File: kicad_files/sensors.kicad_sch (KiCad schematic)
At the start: 41 parts, among them J1 Conn_01x01_Socket, J2 U.FL, U2 MS5611-01BA, U3 BMI088, U4 MMC5983MA, U5 MAX-M10S, U6 BMP388, U7 LSM6DSM

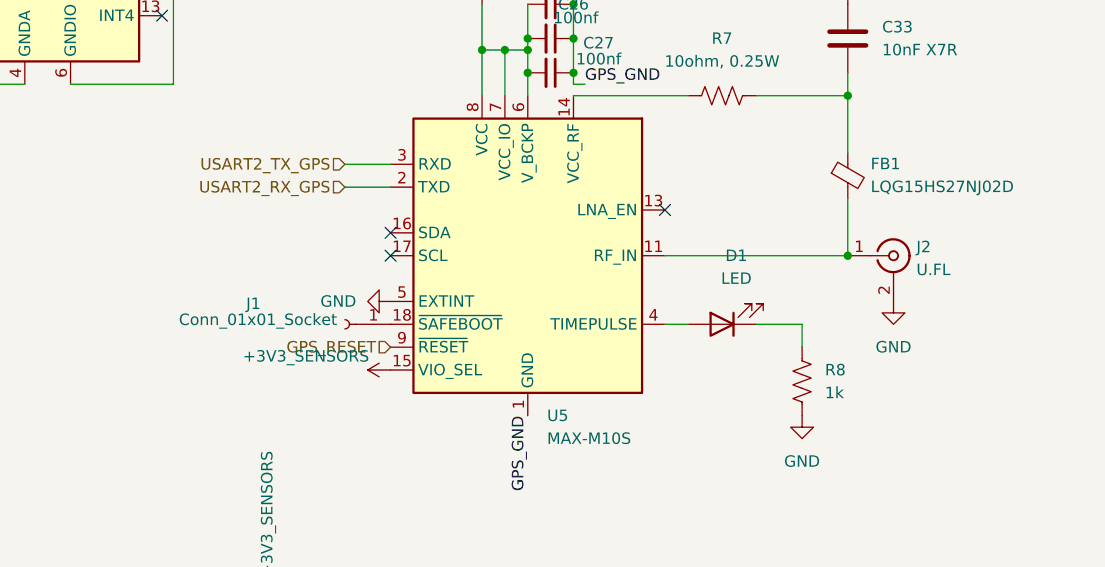
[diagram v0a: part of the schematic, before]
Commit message: size polyfuse, final drc stuff
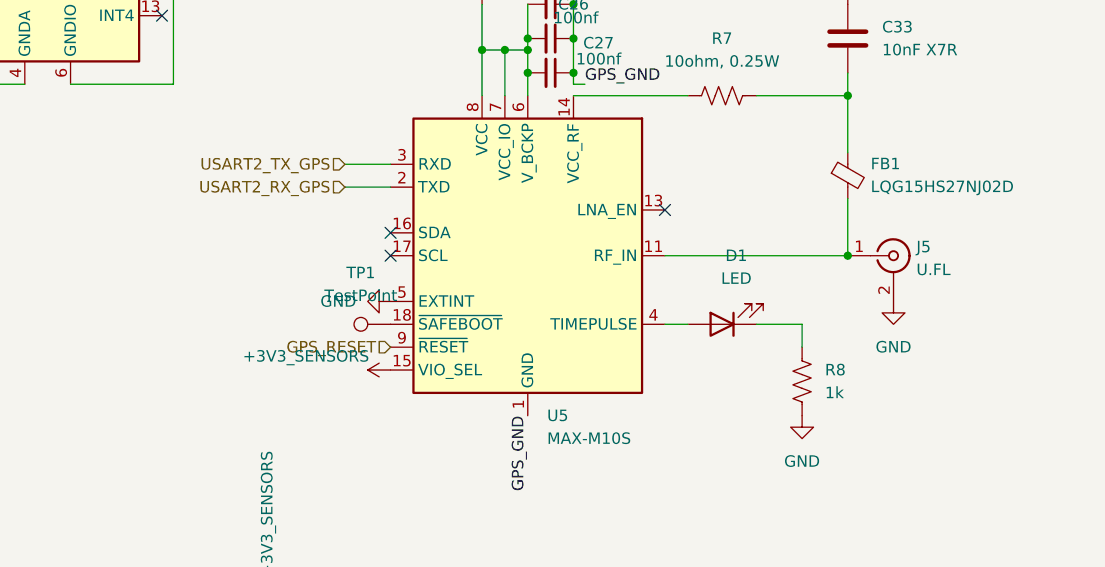
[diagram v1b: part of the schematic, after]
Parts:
- removed J1: Conn_01x01_Socket, TestPoint:TestPoint_Pad_D1.0mm, symbol Connector:Conn_01x01_Socket
- added TP1: TestPoint, TestPoint:TestPoint_Pad_D1.0mm, symbol Connector:TestPoint
- FB2: footprint Resistor_SMD:R_0603_1608Metric -> Inductor_SMD:L_0603_1608Metric
- renumbered J2 to J5
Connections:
- net at U5.18 (~{SAFEBOOT}): now also TP1.1
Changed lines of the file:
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@@
 		(dnp no)
 		(fields_autoplaced yes)
-		(property "Reference" "J2"
+		(property "Reference" "J5"
 			(at 182.88 108.2431 0)
 			(show_name no)
@@
 			(project "versorlite"
 				(path "/1a230af0-0a74-48f7-8607-b087121dda49/11200af7-3897-4179-b08c-df8c2996a93a"
-					(reference "J2")
+					(reference "J5")
 					(unit 1)
 				)
@@
 	)
 	(symbol
+		(lib_id "Connector:TestPoint")
+		(at 124.46 116.84 90)
+		(unit 1)
+		(body_style 1)
+		(exclude_from_sim no)
+		(in_bom yes)
+		(on_board yes)
+		(in_pos_files yes)
+		(dnp no)
+		(fields_autoplaced yes)
+		(property "Reference" "TP1"
+			(at 121.158 111.125 90)
+			(show_name no)
+			(do_not_autoplace no)
+			(effects
+				(font
+					(size 1.27 1.27)
+				)
+			)
+		)
+		(property "Value" "TestPoint"
+			(at 121.158 113.665 90)
+			(show_name no)
+			(do_not_autoplace no)
+			(effects
+				(font
+					(size 1.27 1.27)
+				)
+			)
+		)
+		(property "Footprint" "TestPoint:TestPoint_Pad_D1.0mm"
+			(at 124.46 111.76 0)
+			(hide yes)
+			(show_name no)
+			(do_not_autoplace no)
+			(effects
+				(font
+					(size 1.27 1.27)
+				)
+			)
+		)
+		(property "Datasheet" ""
+			(at 124.46 111.76 0)
+			(hide yes)
+			(show_name no)
+			(do_not_autoplace no)
+			(effects
+				(font
+					(size 1.27 1.27)
+				)
+			)
+		)
+		(property "Description" "test point"
+			(at 124.46 116.84 0)
+			(hide yes)
+			(show_name no)
+			(do_not_autoplace no)
+			(effects
+				(font
+					(size 1.27 1.27)
+				)
+			)
+		)
+		(pin "1"
+		)
+		(instances
+			(project "versorlite"
+				(path "/1a230af0-0a74-48f7-8607-b087121dda49/11200af7-3897-4179-b08c-df8c2996a93a"
+					(reference "TP1")
+					(unit 1)
+				)
+			)
+		)
+	)
+	(symbol
 		(lib_id "Sensor_Motion:BMI088")
 		(at 86.36 74.93 0)
@@
 			)
 		)
-		(property "Footprint" "Resistor_SMD:R_0603_1608Metric"
+		(property "Footprint" "Inductor_SMD:L_0603_1608Metric"
 			(at 229.87 135.382 90)
 			(hide yes)
@@
 					(unit 1)
 				)
-			)
-		)
-	)
-	(symbol
-		(lib_id "Connector:Conn_01x01_Socket")
-		(at 119.38 116.84 180)
-		(unit 1)
-		(body_style 1)
-		(exclude_from_sim no)
-		(in_bom yes)
-		(on_board yes)
-		(in_pos_files yes)
-		(dnp no)
-		(property "Reference" "J1"
-			(at 109.22 114.554 0)
-			(show_name no)
-			(do_not_autoplace no)
-			(effects
-				(font
-					(size 1.27 1.27)
-				)
-			)
-		)
-		(property "Value" "Conn_01x01_Socket"
-			(at 109.728 116.332 0)
-			(show_name no)
-			(do_not_autoplace no)
-			(effects
-				(font
-					(size 1.27 1.27)
-				)
-			)
-		)
-		(property "Footprint" "TestPoint:TestPoint_Pad_D1.0mm"
-			(at 119.38 116.84 0)
-			(hide yes)
-			(show_name no)
-			(do_not_autoplace no)
-			(effects
-				(font
-					(size 1.27 1.27)
-				)
-			)
-		)
-		(property "Datasheet" ""
-			(at 119.38 116.84 0)
-			(hide yes)
-			(show_name no)
-			(do_not_autoplace no)
-			(effects
-				(font
-					(size 1.27 1.27)
-				)
-			)
-		)
-		(property "Description" "Generic connector, single row, 01x01, script generated"
-			(at 119.38 116.84 0)
-			(hide yes)
-			(show_name no)
-			(do_not_autoplace no)
-			(effects
-				(font
-					(size 1.27 1.27)
-				)
-			)
-		)
-		(pin "1"
-		)
-		(instances
-			(project "versorlite"
-				(path "/1a230af0-0a74-48f7-8607-b087121dda49/11200af7-3897-4179-b08c-df8c2996a93a"
-					(reference "J1")
-					(unit 1)
-				)

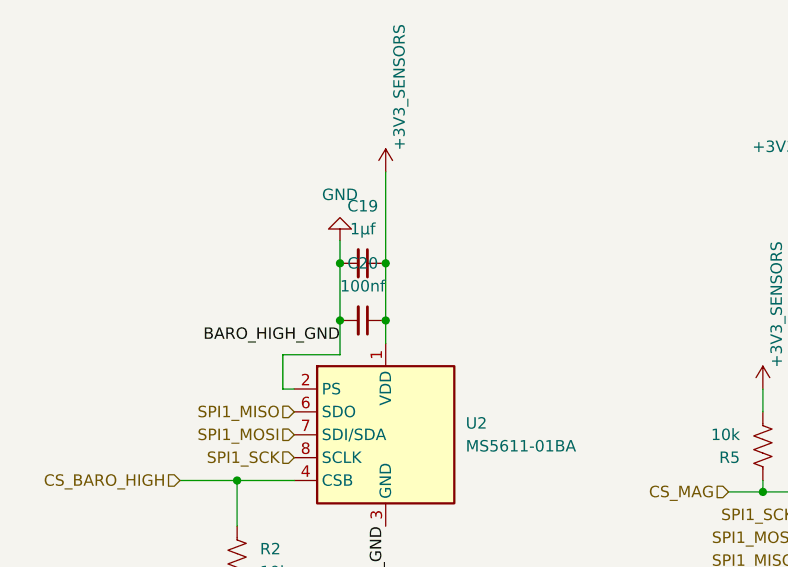
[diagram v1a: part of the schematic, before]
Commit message: better schematic labeling so that mr. dzula isn't confused
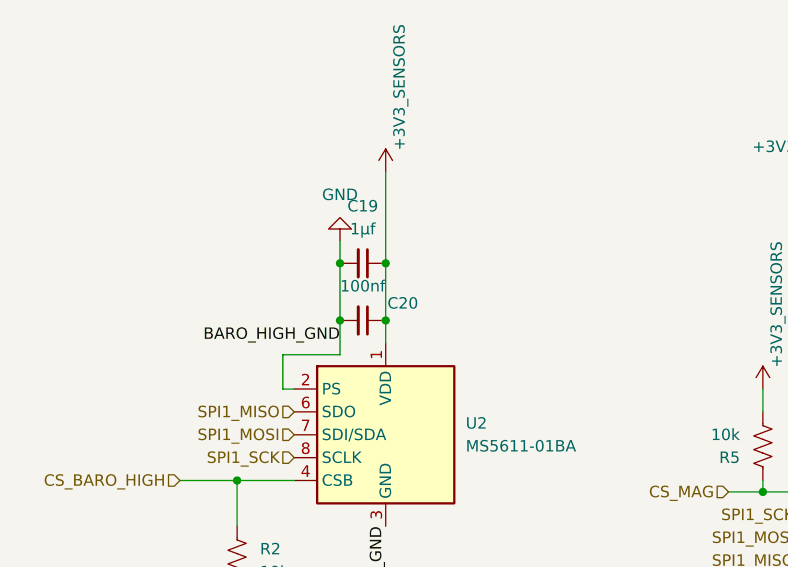
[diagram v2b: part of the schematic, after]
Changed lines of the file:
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@@
 		(in_pos_files yes)
 		(dnp no)
-		(fields_autoplaced yes)
 		(property "Reference" "C20"
-			(at 64.7636 133.35 90)
+			(at 69.215 137.795 90)
 			(show_name no)
 			(do_not_autoplace no)

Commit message: fix pyro adc
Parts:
- renumbered C19 to C17, C20 to C18, C21 to C19, C22 to C20, C23 to C21, C24 to C22, C25 to C23, C26 to C24, C27 to C25, C28 to C26, C29 to C27, C30 to C28, C31 to C29, C32 to C30, C33 to C31, C34 to C32, C35 to C33, C36 to C34, C37 to C35, C38 to C36, C39 to C37, C40 to C38, J5 to J4
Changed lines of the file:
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@@
 		(dnp no)
 		(fields_autoplaced yes)
-		(property "Reference" "C38"
+		(property "Reference" "C36"
 			(at 241.2936 45.72 90)
 			(show_name no)
@@
 			(project "versorlite"
 				(path "/1a230af0-0a74-48f7-8607-b087121dda49/11200af7-3897-4179-b08c-df8c2996a93a"
-					(reference "C38")
+					(reference "C36")
 					(unit 1)
 				)
@@
 		(dnp no)
 		(fields_autoplaced yes)
-		(property "Reference" "J5"
+		(property "Reference" "J4"
 			(at 182.88 108.2431 0)
 			(show_name no)
@@
 			(project "versorlite"
 				(path "/1a230af0-0a74-48f7-8607-b087121dda49/11200af7-3897-4179-b08c-df8c2996a93a"
-					(reference "J5")
+					(reference "J4")
 					(unit 1)
 				)
@@
 		(dnp no)
 		(fields_autoplaced yes)
-		(property "Reference" "C33"
+		(property "Reference" "C31"
 			(at 179.07 83.8199 0)
 			(show_name no)
@@
 			(project "versorlite"
 				(path "/1a230af0-0a74-48f7-8607-b087121dda49/11200af7-3897-4179-b08c-df8c2996a93a"
-					(reference "C33")
+					(reference "C31")
 					(unit 1)
 				)
@@
 		(in_pos_files yes)
 		(dnp no)
-		(property "Reference" "C25"
+		(property "Reference" "C23"
 			(at 142.24 76.962 90)
 			(show_name no)
@@
 			(project "versorlite"
 				(path "/1a230af0-0a74-48f7-8607-b087121dda49/11200af7-3897-4179-b08c-df8c2996a93a"
-					(reference "C25")
+					(reference "C23")
 					(unit 1)
 				)
@@
 		(dnp no)
 		(fields_autoplaced yes)
-		(property "Reference" "C19"
+		(property "Reference" "C17"
 			(at 64.7636 127 90)
 			(show_name no)
@@
 			(project "versorlite"
 				(path "/1a230af0-0a74-48f7-8607-b087121dda49/11200af7-3897-4179-b08c-df8c2996a93a"
-					(reference "C19")
+					(reference "C17")
 					(unit 1)
 				)
@@
 		(in_pos_files yes)
 		(dnp no)
-		(property "Reference" "C27"
+		(property "Reference" "C25"
 			(at 147.574 85.598 90)
 			(show_name no)
@@
 			(project "versorlite"
 				(path "/1a230af0-0a74-48f7-8607-b087121dda49/11200af7-3897-4179-b08c-df8c2996a93a"
-					(reference "C27")
+					(reference "C25")
 					(unit 1)
 				)
@@
 		(dnp no)
 		(fields_autoplaced yes)
-		(property "Reference" "C36"
+		(property "Reference" "C34"
 			(at 223.52 134.6138 0)
 			(show_name no)
@@
 			(project "versorlite"
 				(path "/1a230af0-0a74-48f7-8607-b087121dda49/11200af7-3897-4179-b08c-df8c2996a93a"
-					(reference "C36")
+					(reference "C34")
 					(unit 1)
 				)
@@
 		(in_pos_files yes)
 		(dnp no)
-		(property "Reference" "C34"
+		(property "Reference" "C32"
 			(at 176.53 40.386 90)
 			(show_name no)
@@
 			(project "versorlite"
 				(path "/1a230af0-0a74-48f7-8607-b087121dda49/11200af7-3897-4179-b08c-df8c2996a93a"
-					(reference "C34")
+					(reference "C32")
 					(unit 1)
 				)
@@
 		(dnp no)
 		(fields_autoplaced yes)
-		(property "Reference" "C22"
+		(property "Reference" "C20"
 			(at 81.2736 50.8 90)
 			(show_name no)
@@
 			(project "versorlite"
 				(path "/1a230af0-0a74-48f7-8607-b087121dda49/11200af7-3897-4179-b08c-df8c2996a93a"
-					(reference "C22")
+					(reference "C20")
 					(unit 1)
 				)
@@
 		(dnp no)
 		(fields_autoplaced yes)
-		(property "Reference" "C23"
+		(property "Reference" "C21"
 			(at 91.4336 50.8 90)
 			(show_name no)
@@
 			(project "versorlite"
 				(path "/1a230af0-0a74-48f7-8607-b087121dda49/11200af7-3897-4179-b08c-df8c2996a93a"
-					(reference "C23")
+					(reference "C21")
 					(unit 1)
 				)
@@
 		(dnp no)
 		(fields_autoplaced yes)
-		(property "Reference" "C40"
+		(property "Reference" "C38"
 			(at 251.4536 45.72 90)
 			(show_name no)
@@
 			(project "versorlite"
 				(path "/1a230af0-0a74-48f7-8607-b087121dda49/11200af7-3897-4179-b08c-df8c2996a93a"
-					(reference "C40")
+					(reference "C38")
 					(unit 1)
 				)
@@
 		(in_pos_files yes)
 		(dnp no)
-		(property "Reference" "C24"
+		(property "Reference" "C22"
 			(at 108.204 172.72 0)
 			(show_name no)
@@
 			(project "versorlite"
 				(path "/1a230af0-0a74-48f7-8607-b087121dda49/11200af7-3897-4179-b08c-df8c2996a93a"
-					(reference "C24")
+					(reference "C22")
 					(unit 1)
 				)
@@
 		(in_pos_files yes)
 		(dnp no)
-		(property "Reference" "C32"
+		(property "Reference" "C30"
 			(at 174.498 35.306 90)
 			(show_name no)
@@
 			(project "versorlite"
 				(path "/1a230af0-0a74-48f7-8607-b087121dda49/11200af7-3897-4179-b08c-df8c2996a93a"
-					(reference "C32")
+					(reference "C30")
 					(unit 1)
 				)
@@
 		(dnp no)
 		(fields_autoplaced yes)
-		(property "Reference" "C35"
+		(property "Reference" "C33"
 			(at 184.15 34.2835 0)
 			(show_name no)
@@
 			(project "versorlite"
 				(path "/1a230af0-0a74-48f7-8607-b087121dda49/11200af7-3897-4179-b08c-df8c2996a93a"
-					(reference "C35")
+					(reference "C33")
 					(unit 1)
 				)
@@
 		(dnp no)
 		(fields_autoplaced yes)
-		(property "Reference" "C21"
+		(property "Reference" "C19"
 			(at 81.2736 41.91 90)
 			(show_name no)
@@
 			(project "versorlite"
 				(path "/1a230af0-0a74-48f7-8607-b087121dda49/11200af7-3897-4179-b08c-df8c2996a93a"
-					(reference "C21")
+					(reference "C19")
 					(unit 1)
 				)
@@
 		(dnp no)
 		(fields_autoplaced yes)
-		(property "Reference" "C31"
+		(property "Reference" "C29"
 			(at 170.18 158.7436 90)
 			(show_name no)
@@
 			(project "versorlite"
 				(path "/1a230af0-0a74-48f7-8607-b087121dda49/11200af7-3897-4179-b08c-df8c2996a93a"
-					(reference "C31")
+					(reference "C29")
 					(unit 1)
 				)
@@
 		(dnp no)
 		(fields_autoplaced yes)
-		(property "Reference" "C39"
+		(property "Reference" "C37"
 			(at 251.4536 36.83 90)
 			(show_name no)
@@
 			(project "versorlite"
 				(path "/1a230af0-0a74-48f7-8607-b087121dda49/11200af7-3897-4179-b08c-df8c2996a93a"
-					(reference "C39")
+					(reference "C37")
 					(unit 1)
 				)
@@
 		(dnp no)
 		(fields_autoplaced yes)
-		(property "Reference" "C28"
+		(property "Reference" "C26"
 			(at 161.29 151.1236 90)
 			(show_name no)
@@
 			(project "versorlite"
 				(path "/1a230af0-0a74-48f7-8607-b087121dda49/11200af7-3897-4179-b08c-df8c2996a93a"
-					(reference "C28")
+					(reference "C26")
 					(unit 1)
 				)
@@
 		(dnp no)
 		(fields_autoplaced yes)
-		(property "Reference" "C29"
+		(property "Reference" "C27"
 			(at 161.29 158.7436 90)
 			(show_name no)
@@
 			(project "versorlite"
 				(path "/1a230af0-0a74-48f7-8607-b087121dda49/11200af7-3897-4179-b08c-df8c2996a93a"
-					(reference "C29")
+					(reference "C27")
 					(unit 1)
 				)
@@
 		(in_pos_files yes)
 		(dnp no)
-		(property "Reference" "C26"
+		(property "Reference" "C24"
 			(at 144.78 81.28 90)
 			(show_name no)
@@
 			(project "versorlite"
 				(path "/1a230af0-0a74-48f7-8607-b087121dda49/11200af7-3897-4179-b08c-df8c2996a93a"
-					(reference "C26")
+					(reference "C24")
 					(unit 1)
 				)
@@
 		(dnp no)
 		(fields_autoplaced yes)
-		(property "Reference" "C37"
+		(property "Reference" "C35"
 			(at 241.2936 36.83 90)
 			(show_name no)
@@
 			(project "versorlite"
 				(path "/1a230af0-0a74-48f7-8607-b087121dda49/11200af7-3897-4179-b08c-df8c2996a93a"
-					(reference "C37")
+					(reference "C35")
 					(unit 1)
 				)
@@
 		(in_pos_files yes)
 		(dnp no)
-		(property "Reference" "C20"
+		(property "Reference" "C18"
 			(at 69.215 137.795 90)
 			(show_name no)
@@
 			(project "versorlite"
 				(path "/1a230af0-0a74-48f7-8607-b087121dda49/11200af7-3897-4179-b08c-df8c2996a93a"
-					(reference "C20")
+					(reference "C18")
 					(unit 1)
 				)
@@
 		(dnp no)
 		(fields_autoplaced yes)
-		(property "Reference" "C30"
+		(property "Reference" "C28"
 			(at 170.18 151.1236 90)
 			(show_name no)
@@
 			(project "versorlite"
 				(path "/1a230af0-0a74-48f7-8607-b087121dda49/11200af7-3897-4179-b08c-df8c2996a93a"
-					(reference "C30")
+					(reference "C28")
 					(unit 1)
 				)

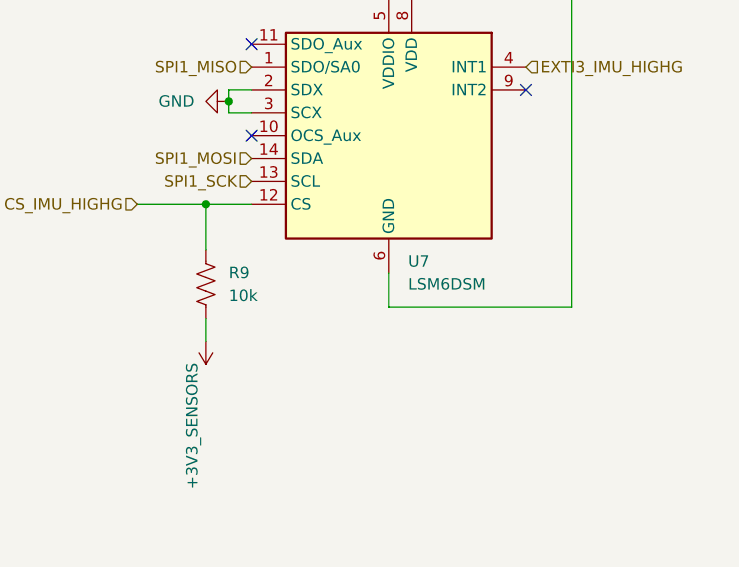
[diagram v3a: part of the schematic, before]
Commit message: replace sensor to lsm6dsv320x
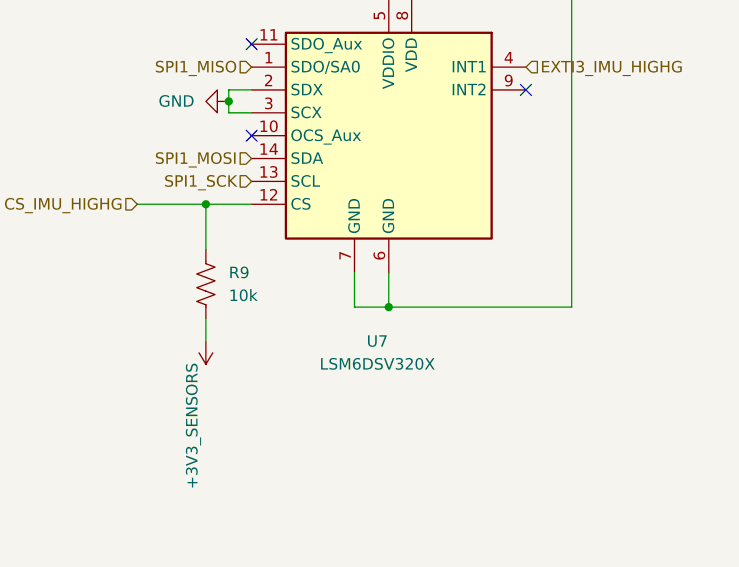
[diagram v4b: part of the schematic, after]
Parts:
- U7: value LSM6DSM -> LSM6DSV320X
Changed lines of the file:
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@@
 	)
 	(junction
+		(at 245.11 91.44)
+		(diameter 0)
+		(color 0 0 0 0)
+	)
+	(junction
 		(at 83.82 48.26)
 		(diameter 0)
@@
 	(wire
 		(pts
+			(xy 241.3 87.63) (xy 241.3 91.44)
+		)
+		(stroke
+			(width 0)
+			(type default)
+		)
+	)
+	(wire
+		(pts
 			(xy 78.74 48.26) (xy 78.74 57.15)
 		)
@@
 	(wire
 		(pts
+			(xy 241.3 91.44) (xy 245.11 91.44)
+		)
+		(stroke
+			(width 0)
+			(type default)
+		)
+	)
+	(wire
+		(pts
 			(xy 165.1 91.44) (xy 175.26 91.44)
 		)
@@
 		(in_pos_files yes)
 		(dnp no)
-		(fields_autoplaced yes)
 		(property "Reference" "U7"
-			(at 247.2533 86.36 0)
+			(at 243.84 95.25 0)
 			(show_name no)
 			(do_not_autoplace no)
@@
 					(size 1.27 1.27)
 				)
-				(justify left)
 			)
 		)
-		(property "Value" "LSM6DSM"
-			(at 247.2533 88.9 0)
+		(property "Value" "LSM6DSV320X"
+			(at 243.84 97.79 0)
 			(show_name no)
 			(do_not_autoplace no)
@@
 					(size 1.27 1.27)
 				)
-				(justify left)
 			)
 		)
@@
 		(pin "4"
 		)
+		(pin "7"
+		)
 		(instances
